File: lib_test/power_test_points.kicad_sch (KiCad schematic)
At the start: 2 parts

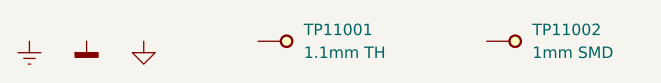
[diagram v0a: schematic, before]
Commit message: add check for 3D models
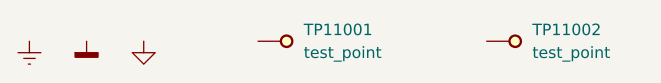
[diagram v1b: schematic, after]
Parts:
- TP11001: value 1.1mm TH -> test_point
- TP11002: value 1mm SMD -> test_point
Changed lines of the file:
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@@
 			)
 		)
-		(property "Value" "1mm SMD"
+		(property "Value" "test_point"
 			(at 81.28 26.67 0)
 			(effects
@@
 			)
 		)
-		(property "Value" "1.1mm TH"
+		(property "Value" "test_point"
 			(at 55.88 26.67 0)
 			(effects

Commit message: add crystal 16MHz
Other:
- company: (none) -> LilyTronics
- title: (none) -> Lily KiCad Library test
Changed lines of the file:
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@@
 	(generator_version "8.0")
 	(paper "A4")
+	(title_block
+		(title "Lily KiCad Library test")
+		(date "2024-07-01")
+		(rev "1")
+		(company "LilyTronics")
+	)
 	(symbol
 		(lib_id "lily_symbols:Earth")
